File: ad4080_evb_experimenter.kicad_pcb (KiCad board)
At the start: 4 copper layers, 104.1 x 91.4 mm, 55 parts, among them J1 Conn_Coaxial, J2 AudioJack2_Ground, J3 Conn_02x02_Odd_Even, J4 Conn_Coaxial, J5 Conn_Coaxial, SW1 SW_Coded_SH-7050, U1 LT1678, U2 74LS163, U3 74HC04, X1 CXO_DIP8

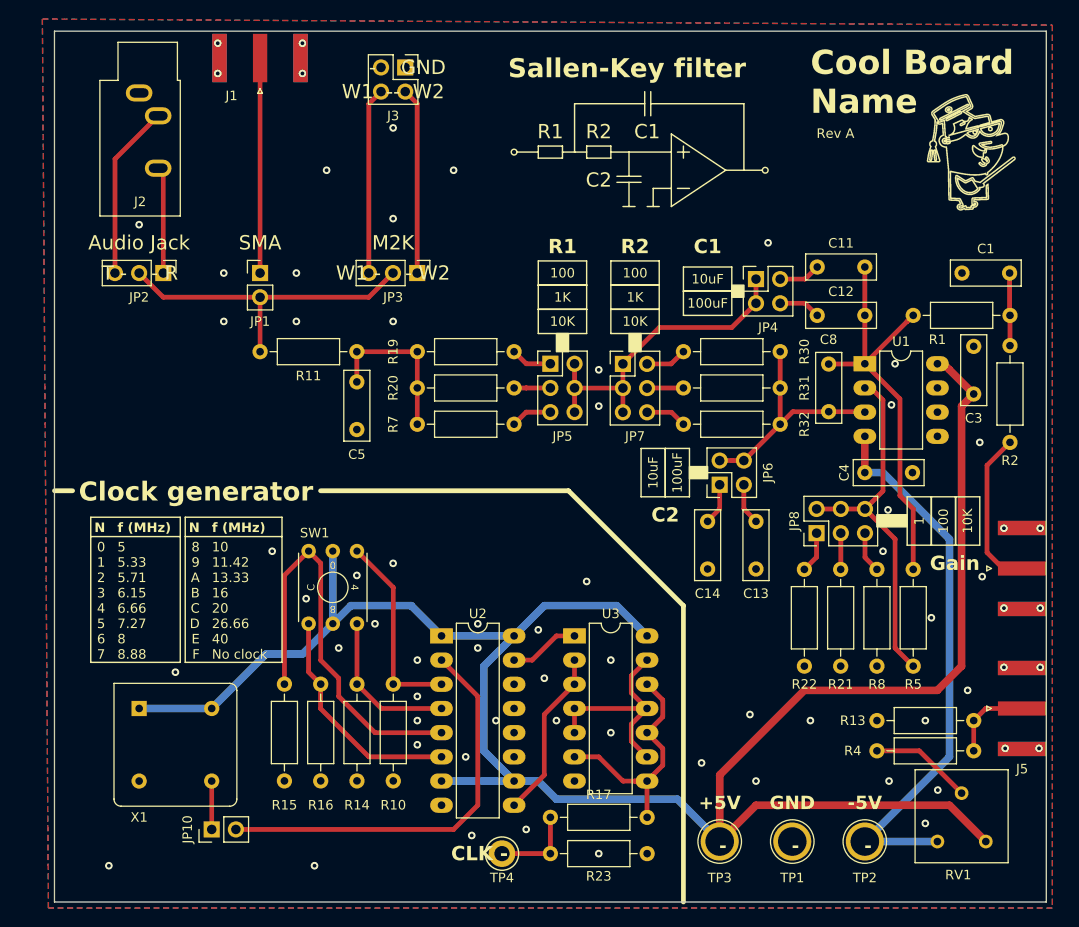
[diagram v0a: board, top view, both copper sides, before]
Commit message: Reduced unused space, fix DRC errors
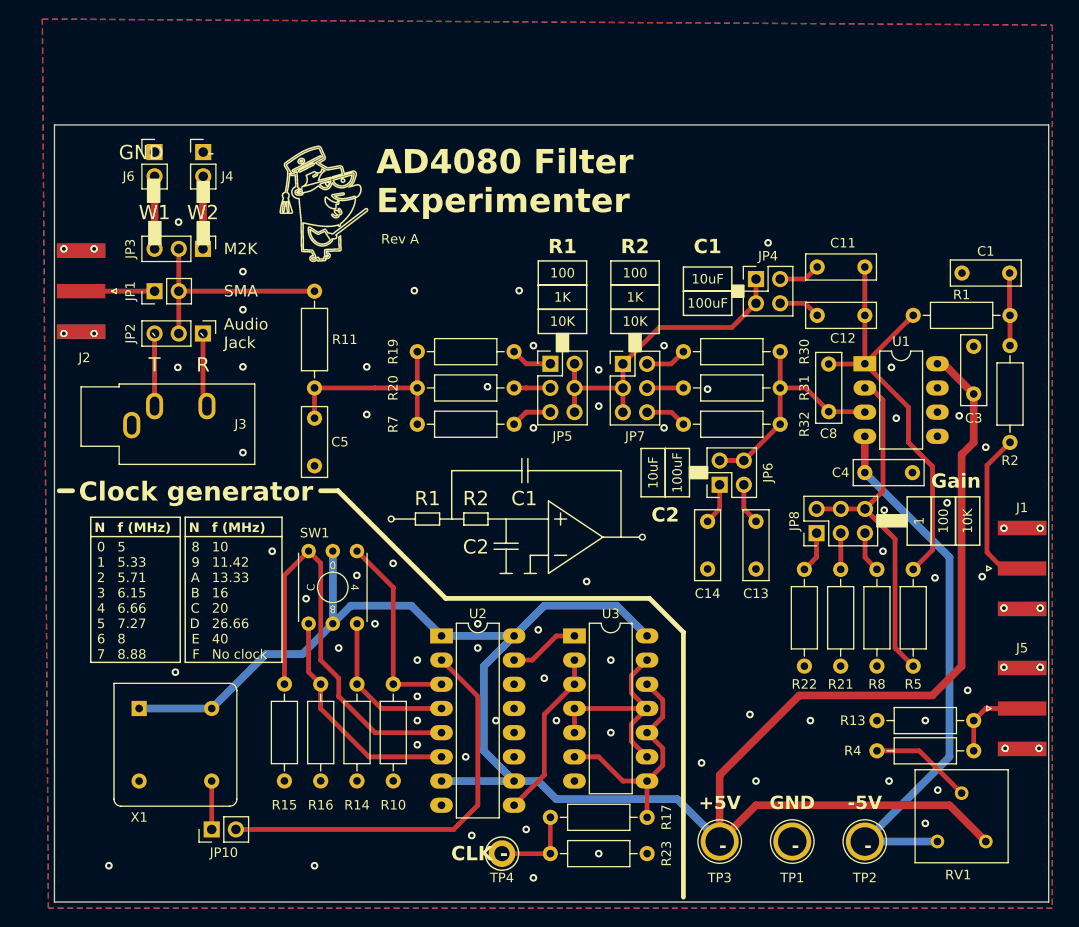
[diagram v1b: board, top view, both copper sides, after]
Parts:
- removed the J3 at (66.0, 35.6)
- added J4: Conn_02x01, Connector_PinHeader_2.54mm:PinHeader_1x02_P2.54mm_Vertical, F.Cu at (44.8, 44.5)
- added J6: Conn_02x01, Connector_PinHeader_2.54mm:PinHeader_1x02_P2.54mm_Vertical, F.Cu at (39.7, 44.5)
- moved REF** 68.2 mm to (57.2, 58.0)
- moved J3 34.9 mm to (37.3, 73.1), turned to 90 degrees
- moved J2 30.9 mm to (32.0, 59.1), turned to 180 degrees
- moved JP3 22.6 mm to (44.8, 54.6)
- moved JP1 11.2 mm to (39.7, 59.1), turned to 90 degrees
- moved R11 8.54 mm to (56.5, 59.1), turned to -90 degrees
- moved JP2 7.59 mm to (44.8, 63.5)
- moved C5 5.85 mm to (56.5, 72.4)
- renumbered J4 to J1, J1 to J2, J2 to J3
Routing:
- net Net-(J2-In): track 22.6 -> 7.97 mm
- net Net-(J4-Pin_2): track 19.6 -> 7.59 mm
- net Net-(J6-Pin_2): track 19.6 -> 7.62 mm
- net Net-(JP1-B): track 34.5 -> 23.1 mm
- net Net-(J3-PadT): track 18.4 -> 7.62 mm
- net Net-(C5-Pad1): track 17.1 -> 21.0 mm
- net Net-(J3-PadR): track 10.5 -> 7.20 mm
- net Net-(C11-Pad2): track 44.8 -> 46.5 mm
- net /V-: track 58.6 -> 57.5 mm
- net Net-(U1A-+): track 24.9 -> 25.5 mm
- net GND: vias 67 -> 76
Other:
- board size 104.1 x 91.4 mm -> 104.4 x 81.6 mm
- board text added: "AD4080 Filter Experimenter"
- board text added: "W1"
- board text added: "W2"
- board text added: "` R"
- board text added: "` T"
- board text removed: "- GND"
- board text removed: "- R"
- board text removed: "- W2"
- board text removed: "Cool Board Name"
- board text removed: "Sallen-Key filter"
- board text removed: "T -"
- board text removed: "W1 -"

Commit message: Single opamp, decouple digital power, selectable attenuation, routing and silkscreen tweaks
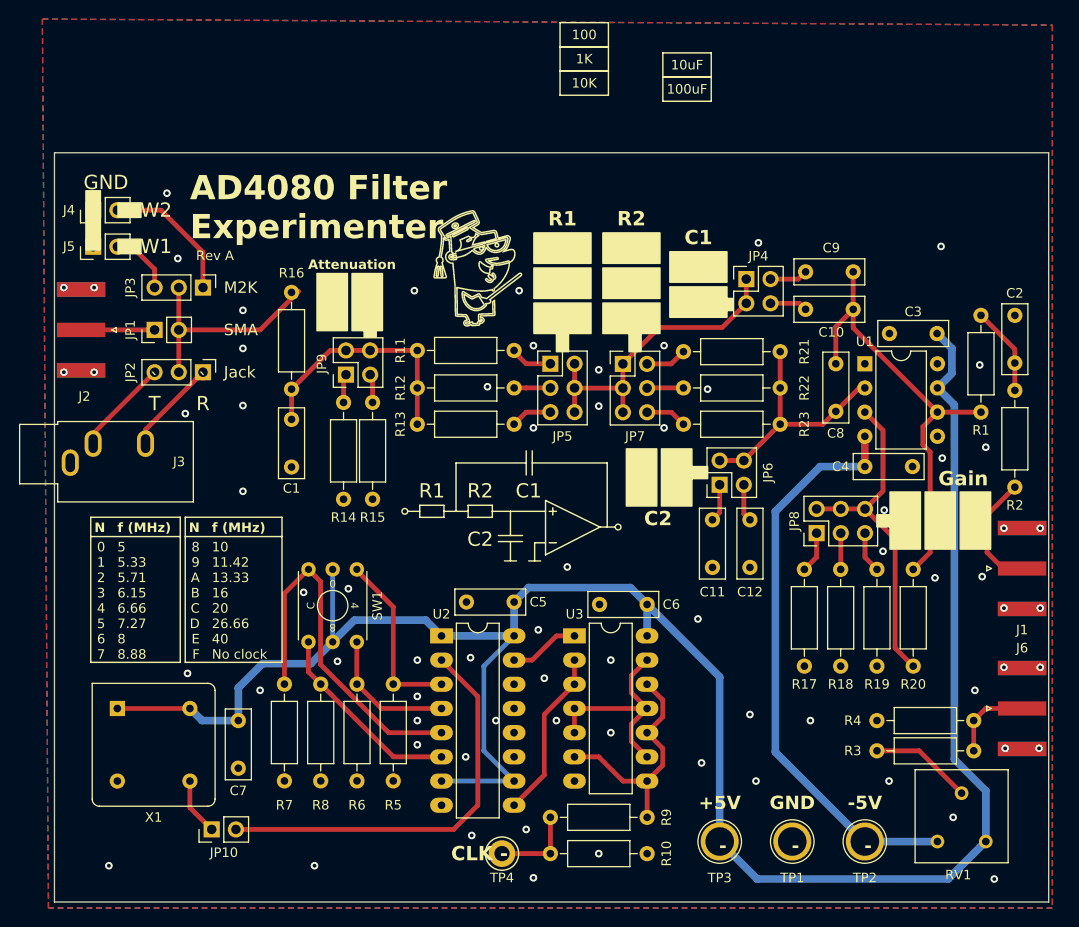
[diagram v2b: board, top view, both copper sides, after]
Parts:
- added C5: 0.1uF, Capacitor_THT:C_Rect_L7.2mm_W2.5mm_P5.00mm_FKS2_FKP2_MKS2_MKP2, F.Cu at (77.5, 91.7)
- added C6: 0.1uF, Capacitor_THT:C_Rect_L7.2mm_W2.5mm_P5.00mm_FKS2_FKP2_MKS2_MKP2, F.Cu at (91.4, 91.9)
- added C7: 0.1uF, Capacitor_THT:C_Rect_L7.2mm_W2.5mm_P5.00mm_FKS2_FKP2_MKS2_MKP2, F.Cu at (48.5, 104.1)
- added JP9: ~, Connector_PinHeader_2.54mm:PinHeader_2x02_P2.54mm_Vertical, F.Cu at (59.8, 67.8)
- added R14: R_US, Resistor_THT:R_Axial_DIN0207_L6.3mm_D2.5mm_P10.16mm_Horizontal, F.Cu at (59.6, 80.9)
- added R15: R_US, Resistor_THT:R_Axial_DIN0207_L6.3mm_D2.5mm_P10.16mm_Horizontal, F.Cu at (62.6, 80.9)
- U1: value LT1678 -> ~; footprint Package_DIP:DIP-8_W7.62mm_LongPads -> Package_DIP:DIP-8_W7.62mm
- moved REF** 17.5 mm to (73.4, 64.8)
- moved J4 13.1 mm to (33.3, 50.5), turned to 90 degrees
- moved R1 12.4 mm to (126.5, 71.8), turned to 90 degrees
- moved J5 11.8 mm to (33.3, 54.4), turned to 90 degrees
- moved C2 9.46 mm to (130.0, 66.6), turned to 90 degrees
- moved J3 7.56 mm to (30.9, 77.1)
- moved C3 7.43 mm to (121.9, 63.5), turned to 180 degrees
- moved R2 4.73 mm to (130.0, 69.5)
- moved J2 4.06 mm to (32.0, 63.1)
- moved JP1 4.06 mm to (39.7, 63.1)
- moved JP3 4.06 mm to (44.8, 58.7)
- moved JP2 4.06 mm to (44.8, 67.6)
- moved R16 2.42 mm to (54.1, 59.2)
- moved C1 2.42 mm to (54.1, 72.5)
- moved X1 2.29 mm to (35.8, 102.9)
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- renumbered C5 to C1, C12 to C10, C14 to C11, C13 to C12, C1 to C2, C11 to C9, J6 to J5, J5 to J6, R23 to R10, R19 to R11, R20 to R12, R7 to R13, R11 to R16, R22 to R17, R21 to R18, R8 to R19, R5 to R20, R30 to R21, R31 to R22, R32 to R23, R4 to R3, R13 to R4, R10 to R5, R14 to R6, R15 to R7, R16 to R8, R17 to R9
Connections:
- C10 pad 2: Net-(C11-Pad2) (its old number) -> Net-(C10-Pad2)
- C8 pad 1: Net-(U1A-+) -> Net-(U1A-V-)
- C8 pad 2: Net-(C11-Pad2) (its old number) -> Net-(C10-Pad2)
- C9 pad 2: Net-(C11-Pad2) (its old number) -> Net-(C10-Pad2)
- JP6 pad 2: Net-(U1A-+) -> Net-(U1A-V-)
- JP6 pad 4: Net-(U1A-+) -> Net-(U1A-V-)
- JP8 pad 2: Net-(U1A--) -> Net-(U1A-V+)
- JP8 pad 4: Net-(U1A--) -> Net-(U1A-V+)
- JP8 pad 6: Net-(U1A--) -> Net-(U1A-V+)
- R1 pad 1: Net-(C11-Pad2) (its old number) -> Net-(C10-Pad2)
- R20 pad 1: Net-(C11-Pad2) (its old number) -> Net-(C10-Pad2)
- R20 pad 2: Net-(U1A--) -> Net-(U1A-V+)
- R21 pad 1: Net-(U1A-+) -> Net-(U1A-V-)
- R22 pad 1: Net-(U1A-+) -> Net-(U1A-V-)
- R23 pad 1: Net-(U1A-+) -> Net-(U1A-V-)
- U1 pad 1: Net-(C11-Pad2) (its old number) -> unconnected-(U1-Pad1)
- U1 pad 2: Net-(U1A--) -> Net-(U1A-V-)
- U1 pad 3: Net-(U1A-+) -> Net-(U1A-V+)
- U1 pad 5: Net-(U1B-+) -> (no net)
- U1 pad 6: Net-(U1B--) -> Net-(C10-Pad2)
- U1 pad 7: Net-(U1-Pad7) -> VCC
- U1 pad 8: VCC -> unconnected-(U1-Pad8)
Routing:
- net Net-(C10-Pad2): track 0.00 -> 47.6 mm
- net Net-(C11-Pad2) (its old number): track 46.5 -> 0.00 mm
- net Net-(U1A--): track 37.7 -> 0.00 mm
- net Net-(U1A-V+): track 0.00 -> 35.4 mm
- net Net-(U1A-V-): track 0.00 -> 26.0 mm
- net Net-(U1A-+): track 25.5 -> 0.00 mm
- net Net-(J4-Pin_2): track 7.59 -> 14.5 mm
- net Net-(C1-Pad1): track 21.0 -> 25.7 mm
- net Net-(U2-D2): track 44.0 -> 39.3 mm
- net Net-(J1-In): track 14.9 -> 10.4 mm
- net Net-(J3-PadR): track 7.20 -> 10.7 mm
- net Net-(U2-D3): track 24.2 -> 20.8 mm
- net /V-: track 57.5 -> 60.7 mm
- net Net-(JP9-Pad1): track 0.00 -> 2.67 mm
- net Net-(JP9-Pad3): track 0.00 -> 2.67 mm
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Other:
- board size 104.4 x 81.6 mm -> 104.4 x 78.7 mm
- board text added: "Attenuation"
- board text added: "GND"
- board text added: "Jack"
- board text removed: "1"
- board text removed: "Audio Jack"
- board text removed: "Clock generator"

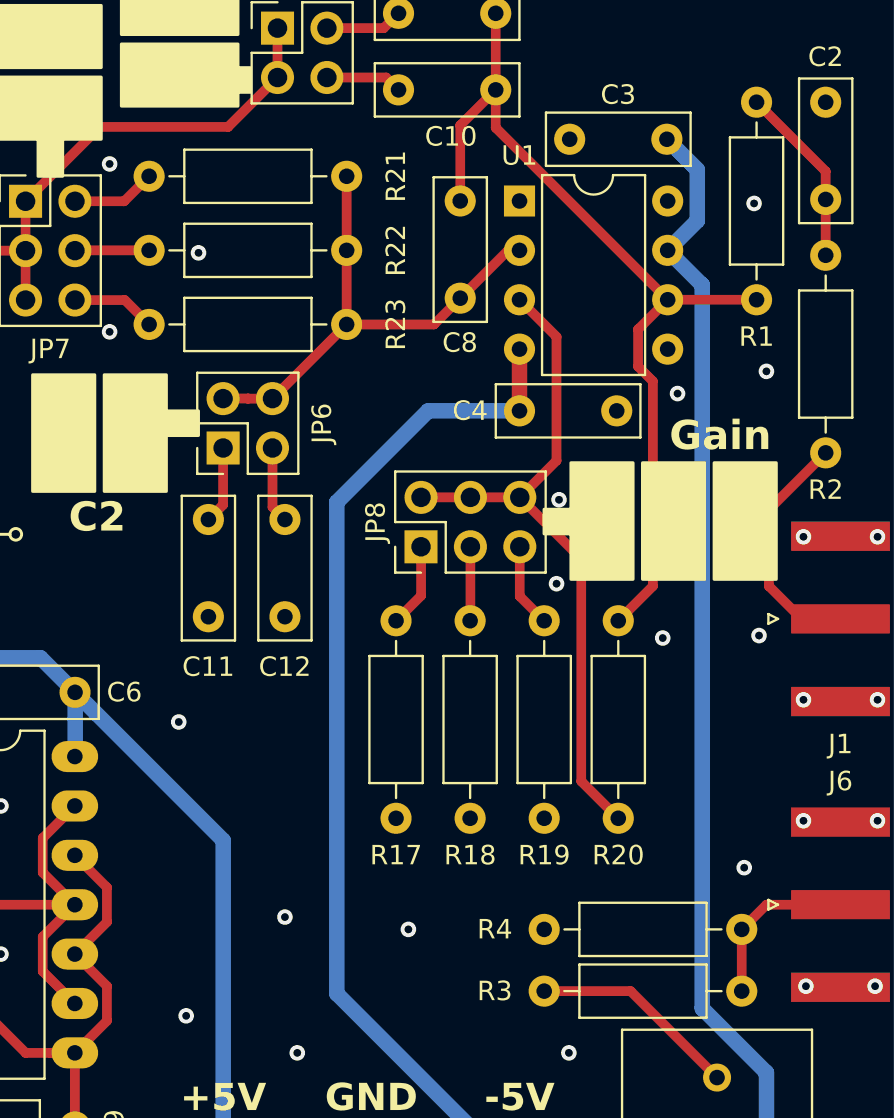
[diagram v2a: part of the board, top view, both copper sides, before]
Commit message: routing tweaks and more vias
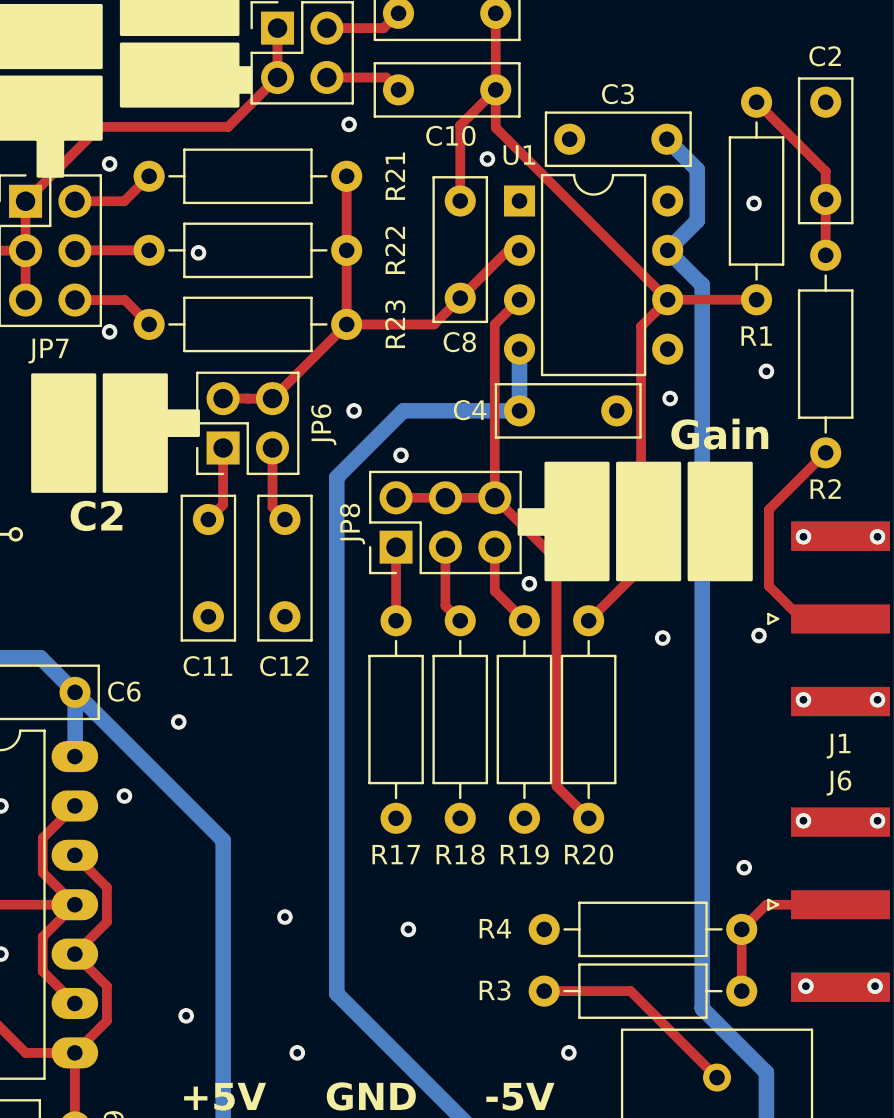
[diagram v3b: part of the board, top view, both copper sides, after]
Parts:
- moved R20 1.52 mm to (117.9, 88.3)
- moved JP8 1.29 mm to (108.0, 84.5)
- moved R19 1.02 mm to (114.6, 98.4)
- moved R18 0.51 mm to (111.3, 98.4)
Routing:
- net Net-(U1A-V+): track 35.4 -> 34.3 mm
- net /V-: track 60.7 -> 61.4 mm
- net Net-(JP8-Pad1): track 4.34 -> 3.78 mm
- net GND: vias 71 -> 75

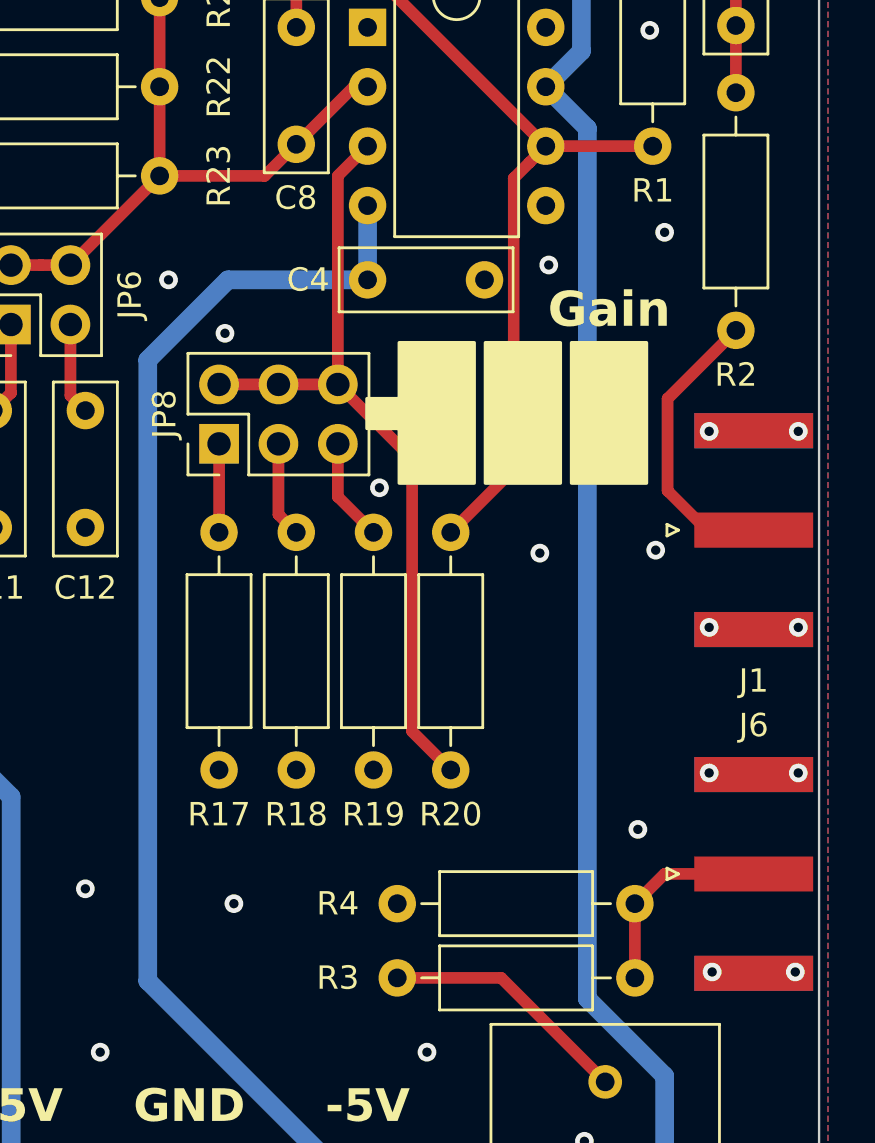
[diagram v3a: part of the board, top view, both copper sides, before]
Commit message: Shrink opamp neg feedback loop
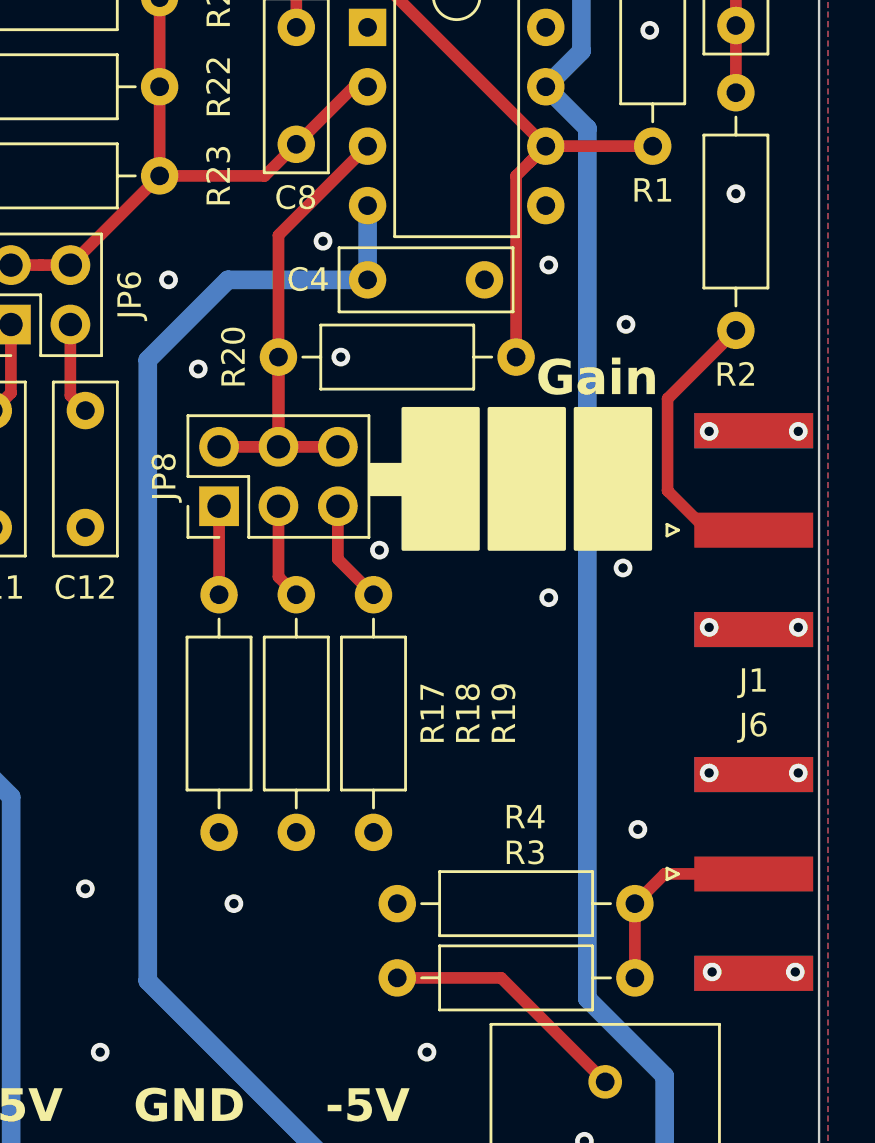
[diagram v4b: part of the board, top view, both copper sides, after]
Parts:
- moved R20 8.00 mm to (120.7, 80.8), turned to 180 degrees
- moved JP8 2.67 mm to (108.0, 87.1)
- moved R17 2.67 mm to (108.0, 101.1)
- moved R18 2.67 mm to (111.3, 101.1)
- moved R19 2.67 mm to (114.6, 101.1)
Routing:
- net Net-(U1A-V+): track 34.3 -> 23.3 mm
- net Net-(C10-Pad2): track 47.6 -> 40.0 mm
- net GND: vias 75 -> 78
